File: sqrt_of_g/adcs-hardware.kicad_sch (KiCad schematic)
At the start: 17 parts, among them J11 Conn_01x20, J12 Conn_01x20, J13 35362-0650, J14 Conn_01x20, J15 353620850, J16 35362-0650, J17 35362-0650, J7 Conn_01x08, J8 Conn_01x20, J9 35362-0650, Q8 IRLML2803, Q9 NDS8434

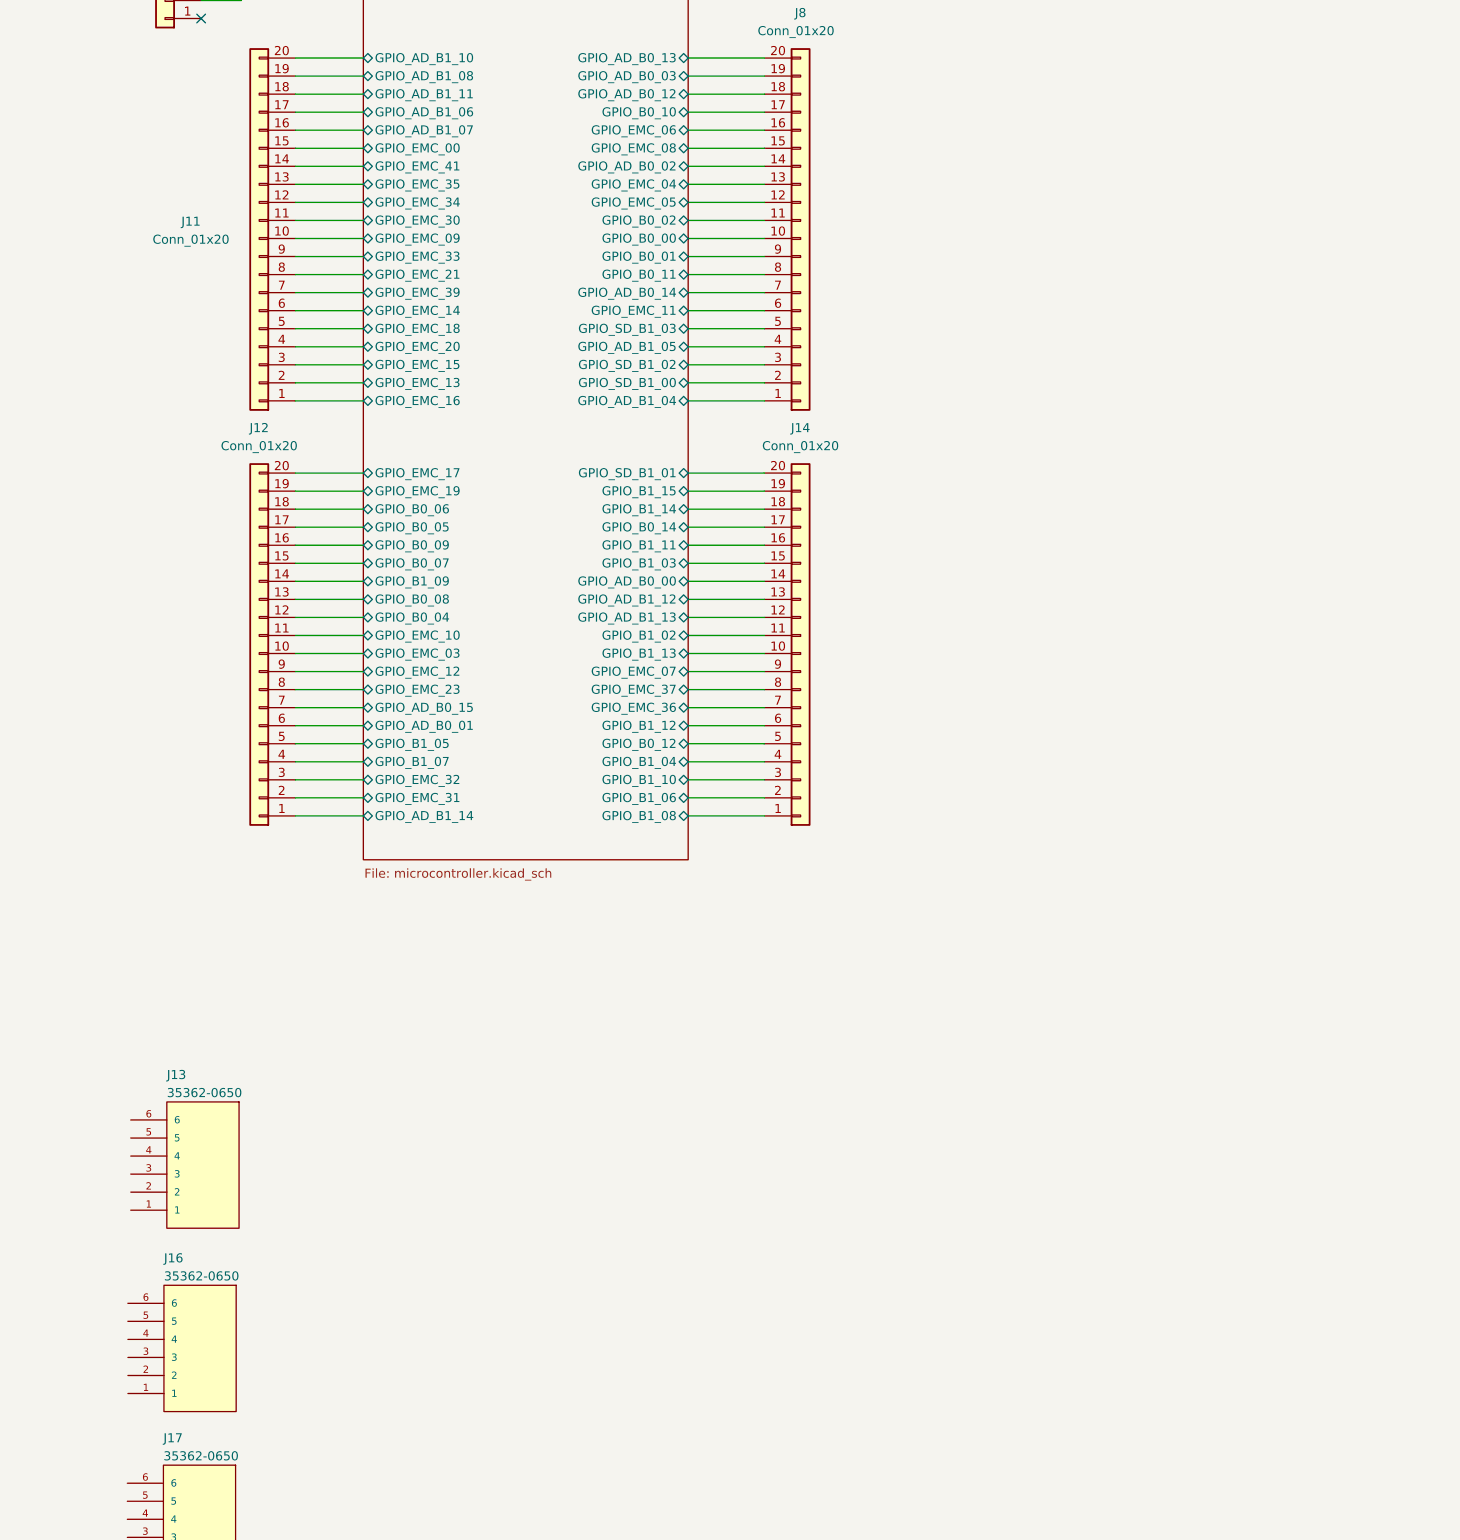
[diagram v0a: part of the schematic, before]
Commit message: move mainboard to subdirectory
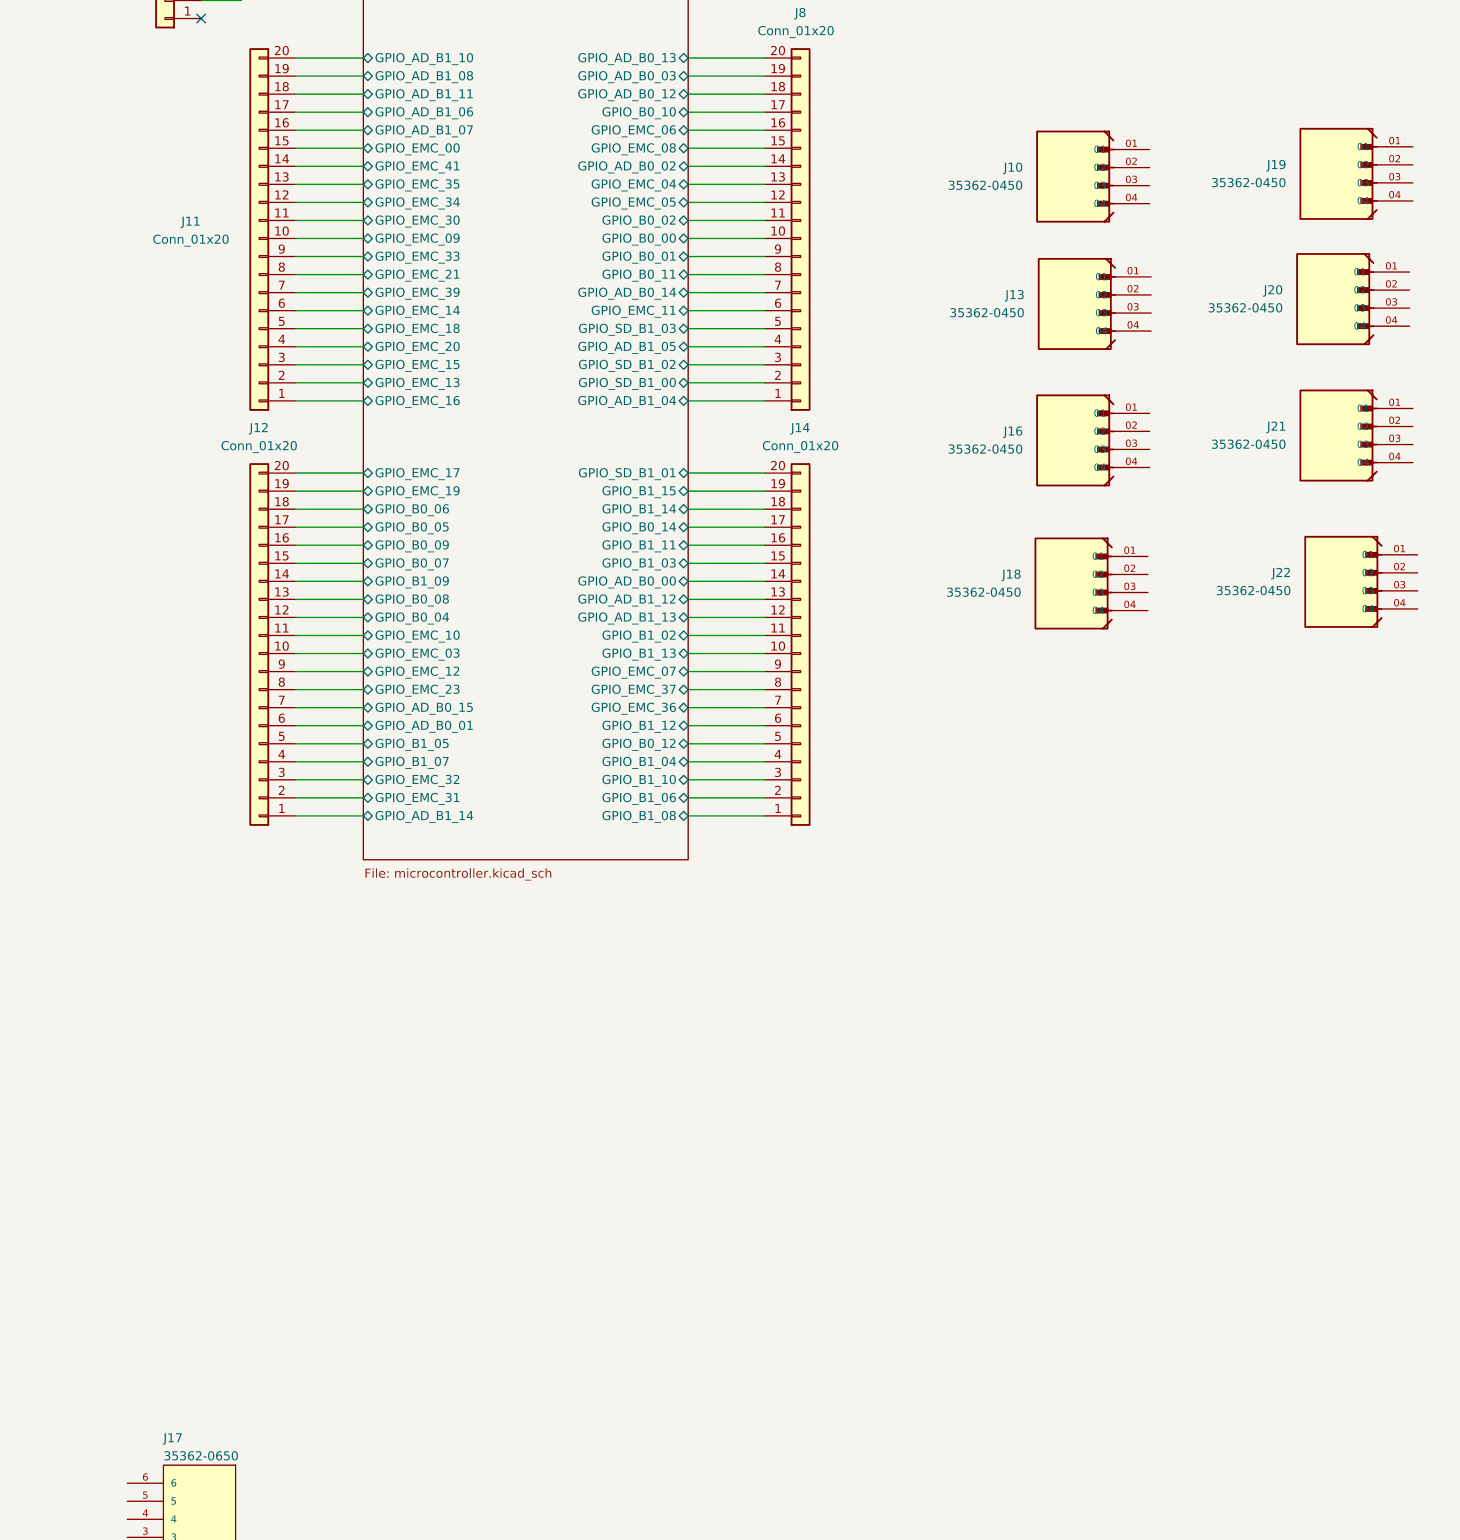
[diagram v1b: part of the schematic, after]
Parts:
- removed J13, J16: 35362-0650, mainboard:MOLEX_35362-0650, symbol mainboard:35362-0650
- added J10, J13, J16, J18, J19, J20, J21, J22: 35362-0450, 35362-0450:MOLEX_35362-0450, symbol adcs:35362-0450

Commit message: more schematic work... I was supposed to finish this a long time ago
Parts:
- removed J10, J13, J16, J18, J19, J20, J21, J22: 35362-0450, 35362-0450:MOLEX_35362-0450, symbol adcs:35362-0450
- removed J12, J14: Conn_01x20, symbol Connector_Generic:Conn_01x20
- removed J17: 35362-0650, mainboard:MOLEX_35362-0650, symbol mainboard:35362-0650
- added J10, J13, J16, J18: 35362-0650, mainboard:MOLEX_35362-0650, symbol mainboard:35362-0650
- added J19, J20: 353621050, CON_353621050, symbol adcs:353621050
- renumbered Q8 to Q1, Q9 to Q2, R31 to R4, R32 to R5, R33 to R6
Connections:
- net MCU/GPIO_B0_00 is gone; now on net MCU/GPIO_EMC_16: J8.10 (Pin_10)
- net MCU/GPIO_B0_01 is gone; now on net MCU/GPIO_EMC_17: J8.9 (Pin_9)
- net MCU/GPIO_B0_02 is gone; now on net MCU/GPIO_EMC_13: J8.11 (Pin_11)
- net MCU/GPIO_EMC_11 is gone; now on net MCU/GPIO_B0_08: J8.6 (Pin_6)
- net GND: now also J10.2, J10.4, J10.6, J13.2, J13.4, J13.6, J16.2, J16.4, J16.6, J18.2, J18.4, J18.6, J19.10, J19.2, J19.4, J19.6, J19.8, J20.10, J20.2, J20.4, J20.6, J20.8
- net MCU/GPIO_AD_B0_00: now also J11.8 (Pin_8)
- net MCU/GPIO_AD_B0_02: now also J8.19 (Pin_19); no longer J8.14 (Pin_14)
- net MCU/GPIO_AD_B0_03: no longer J8.19 (Pin_19)
- net MCU/GPIO_AD_B0_12: now also J13.3; no longer J8.18 (Pin_18)
- net MCU/GPIO_AD_B0_13: now also J13.5; no longer J8.20 (Pin_20)
- net MCU/GPIO_AD_B0_14: now also J18.3; no longer J8.7 (Pin_7)
- net MCU/GPIO_AD_B0_15: now also J18.5
- net MCU/GPIO_AD_B1_04: now also J20.7; no longer J8.1 (Pin_1)
- net MCU/GPIO_AD_B1_05: now also J20.9; no longer J8.4 (Pin_4)
- net MCU/GPIO_AD_B1_06: now also J10.3; no longer J11.17 (Pin_17)
- net MCU/GPIO_AD_B1_07: now also J10.5; no longer J11.16 (Pin_16)
- net MCU/GPIO_AD_B1_08: now also J16.3; no longer J11.19 (Pin_19)
- net MCU/GPIO_AD_B1_09: now also J16.5
- net MCU/GPIO_AD_B1_10: now also J19.3; no longer J11.20 (Pin_20)
- net MCU/GPIO_AD_B1_11: now also J19.5; no longer J11.18 (Pin_18)
- net MCU/GPIO_AD_B1_12: now also J19.7
- net MCU/GPIO_AD_B1_13: now also J19.9
- net MCU/GPIO_AD_B1_14: now also J11.17 (Pin_17)
- net MCU/GPIO_B0_09: now also J8.8 (Pin_8)
- net MCU/GPIO_B0_10: now also J8.20 (Pin_20); no longer J8.17 (Pin_17)
- net MCU/GPIO_B0_11: now also J8.18 (Pin_18); no longer J8.8 (Pin_8)
- net MCU/GPIO_B0_12: now also J11.11 (Pin_11)
- net MCU/GPIO_B0_14: now also J11.20 (Pin_20)
- net MCU/GPIO_B1_02: now also J11.16 (Pin_16)
- net MCU/GPIO_B1_03: now also J11.18 (Pin_18)
- net MCU/GPIO_B1_04: now also J11.10 (Pin_10)
- net MCU/GPIO_B1_05: now also J8.5 (Pin_5)
- net MCU/GPIO_B1_07: now also J8.4 (Pin_4)
- net MCU/GPIO_B1_09: now also J8.7 (Pin_7)
- net MCU/GPIO_B1_10: now also J11.9 (Pin_9)
- net MCU/GPIO_B1_11: now also J11.19 (Pin_19)
- net MCU/GPIO_B1_12: now also J11.12 (Pin_12)
- net MCU/GPIO_B1_13: now also J11.15 (Pin_15)
- net MCU/GPIO_B1_14: now also J8.1 (Pin_1)
- net MCU/GPIO_B1_15: now also J8.2 (Pin_2)
- net MCU/GPIO_EMC_00: no longer J11.15 (Pin_15)
- net MCU/GPIO_EMC_04: no longer J8.13 (Pin_13)
- net MCU/GPIO_EMC_05: no longer J8.12 (Pin_12)
- net MCU/GPIO_EMC_06: no longer J8.16 (Pin_16)
- net MCU/GPIO_EMC_08: no longer J8.15 (Pin_15)
- net MCU/GPIO_EMC_09: no longer J11.10 (Pin_10)
- net MCU/GPIO_EMC_13: no longer J11.2 (Pin_2)
- net MCU/GPIO_EMC_14: now also J8.13 (Pin_13); no longer J11.6 (Pin_6)
- net MCU/GPIO_EMC_15: now also J8.12 (Pin_12); no longer J11.3 (Pin_3)
- net MCU/GPIO_EMC_16: no longer J11.1 (Pin_1)
- net MCU/GPIO_EMC_18: no longer J11.5 (Pin_5)
- net MCU/GPIO_EMC_20: no longer J11.4 (Pin_4)
- net MCU/GPIO_EMC_21: no longer J11.8 (Pin_8)
- net MCU/GPIO_EMC_30: no longer J11.11 (Pin_11)
- net MCU/GPIO_EMC_33: no longer J11.9 (Pin_9)
- net MCU/GPIO_EMC_34: no longer J11.12 (Pin_12)
- net MCU/GPIO_EMC_35: now also J8.14 (Pin_14); no longer J11.13 (Pin_13)
- net MCU/GPIO_EMC_36: now also J11.13 (Pin_13)
- net MCU/GPIO_EMC_37: now also J11.14 (Pin_14)
- net MCU/GPIO_EMC_39: no longer J11.7 (Pin_7)
- net MCU/GPIO_EMC_41: now also J8.15 (Pin_15); no longer J11.14 (Pin_14)
- net MCU/GPIO_SD_B1_00: now also J8.16 (Pin_16); no longer J8.2 (Pin_2)
- net MCU/GPIO_SD_B1_01: now also J8.3 (Pin_3)
- net MCU/GPIO_SD_B1_02: now also J8.17 (Pin_17); no longer J8.3 (Pin_3)
- net MCU/GPIO_SD_B1_03: now also J11.7 (Pin_7); no longer J8.5 (Pin_5)
- new net 3V3_PHOTODIODE1: J10.1, J16.1, J19.1
- new net 3V3_PHOTODIODE2: J13.1, J18.1, J20.1
- new net MCU/GPIO_AD_B1_00: J20.3
- new net MCU/GPIO_AD_B1_01: J20.5
- no-connect marks 2 -> 30
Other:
- removed sheet Sensors
- added sheet GPS (gps.kicad_sch)
- added sheet IMU1_and_MAG1 (imu_and_magnetometer.kicad_sch)
- added sheet IMU2_and_MAG2 (imu_and_magnetometer.kicad_sch)
- added sheet Photodiode_Enable (photodiode_enable.kicad_sch)
- note added: "4 motors x 3 per motor = 12 4 thrusters x 1 per thruster = 4 6 coils x 1 per coil = 6 Total = 22"
- note added: "ADC"
- note added: "LPI2C2"
- note added: "LPI2C4"
- note added: "PWM"
- note removed: "TODO: - switch for connector"
- note removed: "should I put this on the MCU page? - Pete thinks no"
- moved on the sheet: J15, J7

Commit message: ready for 2nd round of reviews
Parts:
- removed C5: 0.1uF, Capacitor_SMD:C_0603_1608Metric, symbol Device:C_Small
- removed C6: 22uF, Capacitor_SMD:C_0603_1608Metric, symbol Device:C_Small
- removed J11, J8: Conn_01x20, symbol Connector_Generic:Conn_01x20
- removed J15: 353620850, mainboard:353620850, symbol Connector_Generic:Conn_01x08
- removed Q1: IRLML2803, mainboard:SOT-23, symbol mainboard:IRLML2803TRPBF
- removed Q2: NDS8434, mainboard:NDS8434, symbol mainboard:NDS8434
- removed R5: 4.7K, Resistor_SMD:R_0603_1608Metric, symbol mainboard:R-US_R0603
- removed R6: 3.3K, Resistor_SMD:R_0603_1608Metric, symbol mainboard:R-US_R0603
- added J11, J15, J17, J27, J8: Conn_01x10, symbol Connector_Generic:Conn_01x10
- added J12: 353620850, mainboard:353620850, symbol Connector_Generic:Conn_01x08
- added J14: 353621050, CON_353621050, symbol adcs:353621050
- added J21, J22, J23, J24, J25, J26: Conn_01x06, symbol Connector_Generic:Conn_01x06
- added J28: 35362-0650, mainboard:MOLEX_35362-0650, symbol mainboard:35362-0650
- added J6: Conn_01x06, Connector_PinHeader_2.54mm:PinHeader_1x06_P2.54mm_Vertical, symbol Connector_Generic:Conn_01x06
- added R27 (x6): 0, Resistor_SMD:R_0603_1608Metric, symbol mainboard:R-US_R0603
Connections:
- net +3V3: now also J21.4 (Pin_4), J22.4 (Pin_4), J23.4 (Pin_4), J24.4 (Pin_4), J25.4 (Pin_4), J26.4 (Pin_4), J27.1 (Pin_1), J28.1, J6.1 (Pin_1)
- net EN_ADCS: now also J7.1 (Pin_1), R4.2, J12.1 (Pin_1), J28.2, J6.2 (Pin_2); no longer J7.8 (Pin_8), R4.1
- net GND: now also J9.1, J9.3, J9.5, R4.1, J11.10 (Pin_10), J14.1, J14.10, J15.10 (Pin_10), J17.10 (Pin_10), J21.3 (Pin_3), J22.3 (Pin_3), J23.3 (Pin_3), J24.3 (Pin_3), J25.3 (Pin_3), J26.3 (Pin_3), J27.10 (Pin_10), J28.4, J6.4 (Pin_4), J8.10 (Pin_10); no longer R4.2
- net MCU/GPIO_AD_B0_01: now also R27.1
- net MCU/GPIO_AD_B0_02: now also J27.4 (Pin_4)
- net MCU/GPIO_AD_B0_03: now also R27.1
- net MCU/GPIO_AD_B1_14: now also J17.5 (Pin_5)
- net MCU/GPIO_B0_08: now also J15.1 (Pin_1)
- net MCU/GPIO_B0_09: now also J15.2 (Pin_2)
- net MCU/GPIO_B0_10: now also J15.3 (Pin_3)
- net MCU/GPIO_B0_11: now also J15.4 (Pin_4)
- net MCU/GPIO_B0_12: now also J15.5 (Pin_5)
- net MCU/GPIO_B0_14: now also J15.6 (Pin_6)
- net MCU/GPIO_B1_02: now also J11.1 (Pin_1)
- net MCU/GPIO_B1_03: now also J11.2 (Pin_2)
- net MCU/GPIO_B1_04: now also J11.3 (Pin_3)
- net MCU/GPIO_B1_05: now also J11.4 (Pin_4)
- net MCU/GPIO_B1_07: now also J11.5 (Pin_5)
- net MCU/GPIO_B1_09: now also J11.6 (Pin_6)
- net MCU/GPIO_B1_10: now also J8.1 (Pin_1)
- net MCU/GPIO_B1_11: now also J8.2 (Pin_2)
- net MCU/GPIO_B1_12: now also J8.3 (Pin_3)
- net MCU/GPIO_B1_13: now also J8.4 (Pin_4)
- net MCU/GPIO_B1_14: now also J8.5 (Pin_5)
- net MCU/GPIO_B1_15: now also J8.6 (Pin_6)
- net MCU/GPIO_EMC_00: now also J8.7 (Pin_7)
- net MCU/GPIO_EMC_03: now also J8.8 (Pin_8)
- net MCU/GPIO_EMC_04: now also J8.9 (Pin_9)
- net MCU/GPIO_EMC_05: now also R27.1
- net MCU/GPIO_EMC_06: now also R27.1
- net MCU/GPIO_EMC_07: now also J14.6
- net MCU/GPIO_EMC_08: now also J14.7
- net MCU/GPIO_EMC_09: now also J14.8
- net MCU/GPIO_EMC_10: now also J14.9
- net MCU/GPIO_EMC_13: now also J14.2
- net MCU/GPIO_EMC_14: now also J14.3
- net MCU/GPIO_EMC_15: now also J14.4
- net MCU/GPIO_EMC_16: now also J14.5
- net MCU/GPIO_EMC_17: now also J27.5 (Pin_5)
- net MCU/GPIO_EMC_18: now also J11.7 (Pin_7)
- net MCU/GPIO_EMC_19: now also J11.8 (Pin_8)
- net MCU/GPIO_EMC_20: now also J11.9 (Pin_9)
- net MCU/GPIO_EMC_21: now also J15.7 (Pin_7)
- net MCU/GPIO_EMC_23: now also J15.8 (Pin_8)
- net MCU/GPIO_EMC_30: now also J15.9 (Pin_9)
- net MCU/GPIO_EMC_31: now also J17.7 (Pin_7)
- net MCU/GPIO_EMC_32: now also J17.8 (Pin_8)
- net MCU/GPIO_EMC_33: now also J17.9 (Pin_9)
- net MCU/GPIO_EMC_34: now also R27.1
- net MCU/GPIO_EMC_35: now also J27.6 (Pin_6)
- net MCU/GPIO_EMC_36: now also J27.7 (Pin_7)
- net MCU/GPIO_EMC_37: now also J27.8 (Pin_8)
- net MCU/GPIO_EMC_39: now also R27.1
- net MCU/GPIO_EMC_41: now also J27.9 (Pin_9)
- net MCU/GPIO_SD_B1_00: now also J17.1 (Pin_1)
- net MCU/GPIO_SD_B1_01: now also J17.2 (Pin_2)
- net MCU/GPIO_SD_B1_02: now also J17.3 (Pin_3)
- net MCU/GPIO_SD_B1_03: now also J17.4 (Pin_4)
- net MCU/ONOFF: now also J7.2 (Pin_2), J12.2 (Pin_2); no longer J7.7 (Pin_7)
- net MCU/PMIC_STBY_REQ: now also J7.4 (Pin_4), J12.4 (Pin_4); no longer J7.5 (Pin_5)
- net MCU/POR_B: now also J7.5 (Pin_5), J12.5 (Pin_5); no longer J7.4 (Pin_4)
- net MCU/WAKEUP: now also J7.3 (Pin_3), J12.3 (Pin_3); no longer J7.6 (Pin_6)
- net RX_ADCS: now also J7.6 (Pin_6), J12.6 (Pin_6); no longer J7.3 (Pin_3)
- net TX_ADCS: now also J7.7 (Pin_7), J12.7 (Pin_7); no longer J7.2 (Pin_2)
- net VBATT: now also J28.5, J6.5 (Pin_5); no longer J9.1, J9.3, J9.5
- net 3V3_PHOTODIODE1 renamed 3V3_PD2
- net 3V3_PHOTODIODE2 renamed 3V3_PD1
- new net: J25.6 (Pin_6), R27.2
- new net: J26.6 (Pin_6), R27.2
- new net: J24.6 (Pin_6), R27.2
- new net: J23.6 (Pin_6), R27.2
- new net: J21.6 (Pin_6), R27.2
- new net: J22.6 (Pin_6), R27.2
- new net +5VD: J28.6, J6.6 (Pin_6)
- new net Coil Power Enable/VBUS_OUT: J21.5 (Pin_5), J22.5 (Pin_5), J23.5 (Pin_5), J24.5 (Pin_5), J25.5 (Pin_5), J26.5 (Pin_5)
- new net GNDREF: J28.3, J6.3 (Pin_3)
- new net MCU/GPIO_AD_B1_15: J17.6 (Pin_6)
- new net MCU/GPIO_SD_B1_04: J27.2 (Pin_2)
- new net MCU/GPIO_SD_B1_05: J27.3 (Pin_3)
- new net SCL2: J22.1 (Pin_1), J23.1 (Pin_1)
- new net SCL4: J21.1 (Pin_1), J24.1 (Pin_1), J25.1 (Pin_1), J26.1 (Pin_1)
- new net SDA2: J22.2 (Pin_2), J23.2 (Pin_2)
- new net SDA4: J21.2 (Pin_2), J24.2 (Pin_2), J25.2 (Pin_2), J26.2 (Pin_2)
- no-connect marks 30 -> 2
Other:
- removed sheet Photodiode_Enable
- added sheet ADCS Power Enable (power_enable.kicad_sch)
- added sheet Coil Power Enable (power_enable.kicad_sch)
- added sheet Photodiode Enable 1 (power_enable.kicad_sch)
- added sheet Photodiode Enable 2 (power_enable.kicad_sch)
- sheet GPS ports: added 3V3_IN; removed none
- sheet IMU1_and_MAG1 ports: added 3V3_IN, EN_SENSORS; removed EN_SENSOR
- sheet IMU2_and_MAG2 ports: added 3V3_IN, EN_SENSORS; removed EN_SENSOR
- sheet MCU ports: added 3V3, GPIO_AD_B1_15, GPIO_SD_B1_04, GPIO_SD_B1_05, VBATT; removed EN_ADCS
- note added: ""EN""
- note added: ""GND""
- note added: ""VUSB""
- note added: "1. Add jumper keep board enabled when operating without PyCubed mainboard"
- note added: "2-3. Add jumper to allow USB battery power to wheels, coils. DO NOT USE TO POWER THRUSTER"
- note added: "A"
- note added: "ADCS Enable"
- note added: "B"
- note added: "C"
- note added: "Coils"
- note added: "Connector allows the RBFs to be placed on a side panel"
- note added: "D"
- note added: "GPIO"
- note added: "GPS"
- note added: "IMU + MAG"
- note added: "LDO for analog 3V3 supply? add inductor, caps to filter things out?"
- note added: "LPI2C1"
- note added: "Photodiodes"
- note added: "PyCubed Mainboard Harness"
- note added: "RBF Jumpers"
- note added: "REMOVE ALL JUMPERS BEFORE FLIGHT"
- note added: "See motors.kicad_sch for work-in-progress motor controller schematic. In the end, we likely do not need all this GPIO per motor."
- note added: "These are set up to either run the current coils, or run new coils that just have h-bridges on them (i.e. by PWM-ing them). The jumpers are to protect the GNC board from Vsolar (which is on the current side panel harnesses)"
- note added: "Thruster"
- note added: "Unclaimed GPIOs"
- note added: "Wheels"
- note added: "X+"
- note added: "X-"
- note added: "Y+"
- note added: "Y-"
- note added: "Z+"
- note added: "Z-"
- note removed: "4 motors x 3 per motor = 12 4 thrusters x 1 per thruster = 4 6 coils x 1 per coil = 6 Total = 22"
- note removed: "ADCS Power Enable"
- moved on the sheet: J10, J13, J16, J18, J19, J20, J9, R4

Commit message: add notes
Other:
- note added: "@GRANT this enable currently has the 3.3K resistor Somewhat related: should it draw from VBATT_IN (to avoid having two enables)? This is already after the foot switches"
- note added: "LDO for analog 3V3 supply? add inductor, caps to filter things out? Should I make an analog GND? I feel like I am fine."
- note removed: "LDO for analog 3V3 supply? add inductor, caps to filter things out?"
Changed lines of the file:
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@@
     (effects (font (size 2.54 2.54)) (justify right bottom))
+  )
+  (text "@GRANT this enable currently has the 3.3K resistor\n\nSomewhat related: should it draw from VBATT_IN (to avoid having two enables)? \nThis is already after the foot switches"
+    (at 207.6196 135.6868 0)
+    (effects (font (size 1.27 1.27) (color 249 0 0 1)) (justify left bottom))
   )
   (text "C" (at 196.3674 310.0324 0)
@@
     (effects (font (size 1.27 1.27)) (justify right bottom))
   )
-  (text "LDO for analog 3V3 supply?\nadd inductor, caps to filter things out?\n"
-    (at 25.4 228.6 0)
+  (text "LDO for analog 3V3 supply?\nadd inductor, caps to filter things out?\n\nShould I make an analog GND? I feel like I am fine.\n"
+    (at -34.2646 238.887 0)
     (effects (font (size 1.27 1.27) (color 255 0 0 1)) (justify left bottom))
   )

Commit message: pete feedback
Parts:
- removed R4: 10K, Resistor_SMD:R_0603_1608Metric, symbol mainboard:R-US_R0603
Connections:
- net EN_ADCS is gone; now on net GND: J12.1 (Pin_1), J28.2, J6.2 (Pin_2), J7.1 (Pin_1)
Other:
- note added: "@GRANT this uses a sheet field to pass in 100k for the source resistor Somewhat related: should we power this from VBATT_IN (to avoid having two enables in series )? This is already after the foot switches"
- note added: "From the board's POV, this is where it recieves and transmits. These must be flipped on the PyCubed side"
- note removed: "@GRANT this enable currently has the 3.3K resistor Somewhat related: should it draw from VBATT_IN (to avoid having two enables)? This is already after the foot switches"
- company: (none) -> Stanford Student Space Initiative
- title: (none) -> √g
